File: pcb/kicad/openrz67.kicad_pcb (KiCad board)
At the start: 2 copper layers, 48 x 22 mm, 59 parts, among them U1 ESP32-C3FH4, U3 LGS5500EP, U4 S4B-XH-A(LF)(SN), U5 TLP172AM, U6 TLP172AM, X1 40MHz, X2 32.768kHz

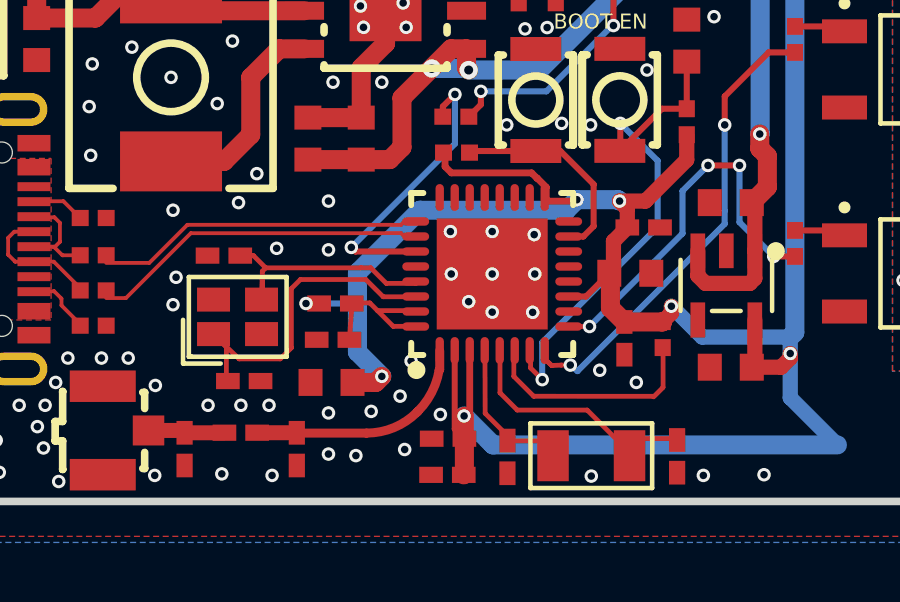
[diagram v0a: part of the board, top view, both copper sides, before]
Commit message: PCB rev 2: apply pre-fab review fixes
Blockers from the 2026-09-07 review:
- R11 100k -> 10k. It sets the LGS5500 charge current; 100k meant 1 A into
  the 250 mAh cell (rev 1 shipped like that). 10k = 400 mA per datasheet.
- Three resistor lines had 19-40 pieces in JLCPCB stock: 10k group ->
  C25744 (Basic), R12 1k -> C21190 (Basic), R18 3k -> C2909355. Library
  symbols renamed to the new MPNs, 100k symbol dropped, board fields synced.
- The VCC via feeding L2 pad 1 had its hole 0.083 mm inside the pad copper;
  moved 0.55 mm below the pad with a short F.Cu stub.

Should-fixes:
- openrz67.kicad_dru: two scoped rules instead of one unscoped one, so the
  pours stay 0.25 mm off the USB1 peg holes (rev-1 geometry) while USB1's
  own pads keep 0.17 mm.
- regen.sh: gerbers and drill use the aux origin like the CPL, so the drill
  files diff directly against the rev-1 archive; CPL rotations 0-359;
  BOM written with JLCPCB's column names and no library prefix.
- S1_DRV via nudged 0.15 mm off U1 pad 9; VDDA added to the 3v net class.

DRC 0 errors / 9 known warnings, ERC 0/0, parity clean. Every non-via
drill hole matches the rev-1 archive.
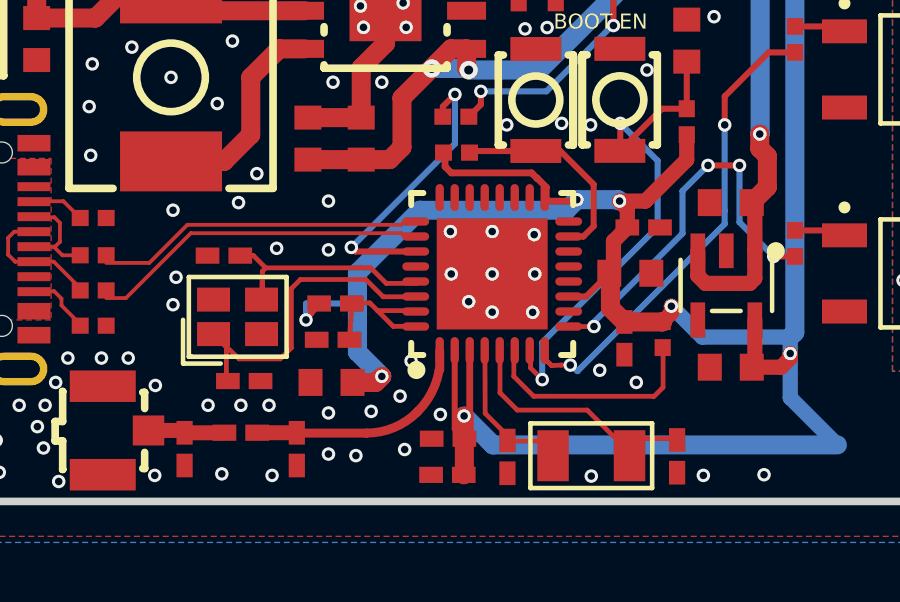
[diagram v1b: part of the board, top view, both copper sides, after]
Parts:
- R11: value 100kΩ -> 10kΩ
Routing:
- net VCC: track 93.4 -> 94.7 mm
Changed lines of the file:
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@@
 			)
 		)
-		(property "Datasheet" "https://atta.szlcsc.com/upload/public/pdf/source/20170925/C131467_1506321478108990263.pdf"
+		(property "Datasheet" "https://www.lcsc.com/product-detail/C25744.html"
 			(at 0 0 270)
 			(layer "F.Fab")
@@
 			)
 		)
-		(property "Manufacturer" "YAGEO(国巨)"
+		(property "Manufacturer" "UNI-ROYAL(厚声)"
 			(at 0 0 0)
 			(layer "F.Fab")
@@
 			)
 		)
-		(property "Manufacturer Part" "RC0402FR-0710KL"
+		(property "Manufacturer Part" "0402WGF1002TCE"
 			(at 0 0 0)
 			(layer "F.Fab")
@@
 			)
 		)
-		(property "Supplier Part" "C60490"
+		(property "Supplier Part" "C25744"
 			(at 0 0 0)
 			(layer "F.Fab")
@@
 			)
 		)
-		(property "LCSC Part Name" "厚膜电阻 10kΩ ±1% 62.5mW"
+		(property "LCSC Part Name" "10kΩ ±1% 62.5mW 厚膜电阻"
 			(at 0 0 0)
 			(layer "F.Fab")
@@
 			)
 		)
-		(property "Datasheet" "https://atta.szlcsc.com/upload/public/pdf/source/20170925/C131467_1506321478108990263.pdf"
+		(property "Datasheet" "https://www.lcsc.com/product-detail/C25744.html"
 			(at 0 0 90)
 			(layer "F.Fab")
@@
 			)
 		)
-		(property "Manufacturer" "YAGEO(国巨)"
+		(property "Manufacturer" "UNI-ROYAL(厚声)"
 			(at 0 0 0)
 			(layer "F.Fab")
@@
 			)
 		)
-		(property "Manufacturer Part" "RC0402FR-0710KL"
+		(property "Manufacturer Part" "0402WGF1002TCE"
 			(at 0 0 0)
 			(layer "F.Fab")
@@
 			)
 		)
-		(property "Supplier Part" "C60490"
+		(property "Supplier Part" "C25744"
 			(at 0 0 0)
 			(layer "F.Fab")
@@
 			)
 		)
-		(property "LCSC Part Name" "厚膜电阻 10kΩ ±1% 62.5mW"
+		(property "LCSC Part Name" "10kΩ ±1% 62.5mW 厚膜电阻"
 			(at 0 0 0)
 			(layer "F.Fab")
@@
 			)
 		)
-		(property "Datasheet" "https://atta.szlcsc.com/upload/public/pdf/source/20170925/C131467_1506321478108990263.pdf"
+		(property "Datasheet" "https://www.lcsc.com/product-detail/C25744.html"
 			(at 0 0 90)
 			(layer "F.Fab")
@@
 			)
 		)
-		(property "Manufacturer" "YAGEO(国巨)"
+		(property "Manufacturer" "UNI-ROYAL(厚声)"
 			(at 0 0 0)
 			(layer "F.Fab")
@@
 			)
 		)
-		(property "Manufacturer Part" "RC0402FR-0710KL"
+		(property "Manufacturer Part" "0402WGF1002TCE"
 			(at 0 0 0)
 			(layer "F.Fab")
@@
 			)
 		)
-		(property "Supplier Part" "C60490"
+		(property "Supplier Part" "C25744"
 			(at 0 0 0)
 			(layer "F.Fab")
@@
 			)
 		)
-		(property "LCSC Part Name" "厚膜电阻 10kΩ ±1% 62.5mW"
+		(property "LCSC Part Name" "10kΩ ±1% 62.5mW 厚膜电阻"
 			(at 0 0 0)
 			(layer "F.Fab")
@@
 			)
 		)
-		(property "Datasheet" "https://atta.szlcsc.com/upload/public/pdf/source/20170925/C131467_1506321478108990263.pdf"
+		(property "Datasheet" "https://www.lcsc.com/product-detail/C25744.html"
 			(at 0 0 0)
 			(layer "F.Fab")
@@
 			)
 		)
-		(property "Manufacturer" "YAGEO(国巨)"
+		(property "Manufacturer" "UNI-ROYAL(厚声)"
 			(at 0 0 0)
 			(layer "F.Fab")
@@
 			)
 		)
-		(property "Manufacturer Part" "RC0402FR-0710KL"
+		(property "Manufacturer Part" "0402WGF1002TCE"
 			(at 0 0 0)
 			(layer "F.Fab")
@@
 			)
 		)
-		(property "Supplier Part" "C60490"
+		(property "Supplier Part" "C25744"
 			(at 0 0 0)
 			(layer "F.Fab")
@@
 			)
 		)
-		(property "LCSC Part Name" "厚膜电阻 10kΩ ±1% 62.5mW"
+		(property "LCSC Part Name" "10kΩ ±1% 62.5mW 厚膜电阻"
 			(at 0 0 0)
 			(layer "F.Fab")
@@
 			)
 		)
-		(property "Datasheet" "https://atta.szlcsc.com/upload/public/pdf/source/20170925/C131467_1506321478108990263.pdf"
+		(property "Datasheet" "https://www.lcsc.com/product-detail/C25744.html"
 			(at 0 0 270)
 			(layer "F.Fab")
@@
 			)
 		)
-		(property "Manufacturer" "YAGEO(国巨)"
+		(property "Manufacturer" "UNI-ROYAL(厚声)"
 			(at 0 0 0)
 			(layer "F.Fab")
@@
 			)
 		)
-		(property "Manufacturer Part" "RC0402FR-0710KL"
+		(property "Manufacturer Part" "0402WGF1002TCE"
 			(at 0 0 0)
 			(layer "F.Fab")
@@
 			)
 		)
-		(property "Supplier Part" "C60490"
+		(property "Supplier Part" "C25744"
 			(at 0 0 0)
 			(layer "F.Fab")
@@
 			)
 		)
-		(property "LCSC Part Name" "厚膜电阻 10kΩ ±1% 62.5mW"
+		(property "LCSC Part Name" "10kΩ ±1% 62.5mW 厚膜电阻"
 			(at 0 0 0)
 			(layer "F.Fab")
@@
 			)
 		)
-		(property "Datasheet" "https://atta.szlcsc.com/upload/public/pdf/source/20170925/C131467_1506321478108990263.pdf"
+		(property "Datasheet" "https://www.lcsc.com/product-detail/C25744.html"
 			(at 0 0 180)
 			(layer "F.Fab")
@@
 			)
 		)
-		(property "Manufacturer" "YAGEO(国巨)"
+		(property "Manufacturer" "UNI-ROYAL(厚声)"
 			(at 0 0 0)
 			(layer "F.Fab")
@@
 			)
 		)
-		(property "Manufacturer Part" "RC0402FR-0710KL"
+		(property "Manufacturer Part" "0402WGF1002TCE"
 			(at 0 0 0)
 			(layer "F.Fab")
@@
 			)
 		)
-		(property "Supplier Part" "C60490"
+		(property "Supplier Part" "C25744"
 			(at 0 0 0)
 			(layer "F.Fab")
@@
 			)
 		)
-		(property "LCSC Part Name" "厚膜电阻 10kΩ ±1% 62.5mW"
+		(property "LCSC Part Name" "10kΩ ±1% 62.5mW 厚膜电阻"
 			(at 0 0 0)
 			(layer "F.Fab")
@@
 			)
 		)
-		(property "Datasheet" "https://atta.szlcsc.com/upload/public/pdf/source/20170925/C131467_1506321478108990263.pdf"
+		(property "Datasheet" "https://www.lcsc.com/product-detail/C25744.html"
 			(at 0 0 0)
 			(layer "F.Fab")
@@
 			)
 		)
-		(property "Manufacturer" "YAGEO(国巨)"
+		(property "Manufacturer" "UNI-ROYAL(厚声)"
 			(at 0 0 0)
 			(layer "F.Fab")
@@
 			)
 		)
-		(property "Manufacturer Part" "RC0402FR-0710KL"
+		(property "Manufacturer Part" "0402WGF1002TCE"
 			(at 0 0 0)
 			(layer "F.Fab")
@@
 			)
 		)
-		(property "Supplier Part" "C60490"
+		(property "Supplier Part" "C25744"
 			(at 0 0 0)
 			(layer "F.Fab")
@@
 			)
 		)
-		(property "LCSC Part Name" "厚膜电阻 10kΩ ±1% 62.5mW"
+		(property "LCSC Part Name" "10kΩ ±1% 62.5mW 厚膜电阻"
 			(at 0 0 0)
 			(layer "F.Fab")
@@
 			)
 		)
-		(property "Datasheet" "https://atta.szlcsc.com/upload/public/pdf/source/20200306/C422600_1E6D84923E4A46A82E41ADD87F860B5C.pdf"
+		(property "Datasheet" "https://www.lcsc.com/product-detail/C2909355.html"
 			(at 0 0 90)
 			(layer "F.Fab")
@@
 			)
 		)
-		(property "Description" "Type:Thick Film Resistors Resistance:3kΩ Tolerance:±1% Tolerance:±1% Power(Watts): Overload Voltage (Max): Temperature Coefficient:±100ppm/℃ Temperature Coefficient:±100ppm/℃ Operating Temperature Range:-55℃~+155℃ Operating Temperature Range:-55℃~+155℃"
+		(property "Description" ""
 			(at 0 0 90)
 			(layer "F.Fab")
@@
 			)
 		)
-		(property "Manufacturer" "UNI-ROYAL(厚声)"
+		(property "Manufacturer" "FOJAN"
 			(at 0 0 0)
 			(layer "F.Fab")
@@
 			)
 		)
-		(property "Manufacturer Part" "0402WGF3001TCE"
+		(property "Manufacturer Part" "FRC0402F3001TS"
 			(at 0 0 0)
 			(layer "F.Fab")
@@
 			)
 		)
-		(property "Supplier Part" "C25784"
+		(property "Supplier Part" "C2909355"
 			(at 0 0 0)
 			(layer "F.Fab")
@@
 			)
 		)
-		(property "Datasheet" "https://item.szlcsc.com/datasheet/0603WAJ0102T5E/26328.html"
+		(property "Datasheet" "https://www.lcsc.com/product-detail/C21190.html"
 			(at 0 0 270)
 			(layer "F.Fab")
@@
 			)
 		)
-		(property "Manufacturer Part" "0603WAJ0102T5E"
+		(property "Manufacturer Part" "0603WAF1001T5E"
 			(at 0 0 0)
 			(layer "F.Fab")
@@
 			)
 		)
-		(property "Supplier Part" "C25585"
+		(property "Supplier Part" "C21190"
 			(at 0 0 0)
 			(layer "F.Fab")
@@
 			)
 		)
-		(property "LCSC Part Name" "1kΩ ±5% 100mW 厚膜电阻"
+		(property "LCSC Part Name" "1kΩ ±1% 100mW 厚膜电阻"
 			(at 0 0 0)
 			(layer "F.Fab")
@@
 			)
 		)
-		(property "Value" "100kΩ"
+		(property "Value" "10kΩ"
 			(at 0 0 270)
 			(layer "F.Fab")
@@
 			)
 		)
-		(property "Datasheet" "https://item.szlcsc.com/datasheet/0402WGF1003TCE/26484.html"
+		(property "Datasheet" "https://www.lcsc.com/product-detail/C25744.html"
 			(at 0 0 270)
 			(layer "F.Fab")
@@
 			)
 		)
-		(property "Manufacturer Part" "0402WGF1003TCE"
+		(property "Manufacturer Part" "0402WGF1002TCE"
 			(at 0 0 0)
 			(layer "F.Fab")
@@
 			)
 		)
-		(property "Supplier Part" "C25741"
+		(property "Supplier Part" "C25744"
 			(at 0 0 0)
 			(layer "F.Fab")
@@
 			)
 		)
-		(property "LCSC Part Name" "100kΩ ±1% 62.5mW 厚膜电阻"
+		(property "LCSC Part Name" "10kΩ ±1% 62.5mW 厚膜电阻"
 			(at 0 0 0)
 			(layer "F.Fab")
@@
 	)
 	(segment
+		(start 135.05 105.95)
+		(end 135.487 105.4025)
+		(width 0.2)
+		(layer "F.Cu")
+		(net "VCC")
+	)
+	(segment
 		(start 144.2275 93.6535)
 		(end 144.2825 93.7085)
@@
 	)
 	(via
-		(at 135.05 105.4025)
+		(at 135.05 105.95)
 		(size 0.45)
 		(drill 0.25)
@@
 	)
 	(segment
+		(start 135.05 105.95)
+		(end 135.05 105.4025)
+		(width 0.2)
+		(layer "B.Cu")
+		(net "VCC")
+	)
+	(segment
 		(start 144.079 101.942)
 		(end 145.4545 101.942)
@@
 	(segment
 		(start 143.807 106.1695)
-		(end 144.5 106.1695)
+		(end 144.65 106.1695)
 		(width 0.16)
 		(layer "F.Cu")
@@
 	)
 	(via
-		(at 144.5 106.1695)
+		(at 144.65 106.1695)
 		(size 0.45)
 		(drill 0.25)
@@
 		(net "S1_DRV")
 	)
+	(segment
+		(start 144.65 106.1695)
+		(end 144.5 106.1695)
+		(width 0.203)
+		(layer "B.Cu")
+		(net "S1_DRV")
+	)

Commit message: PCB: unpopulated 1x4 GPIO header J1 along the bottom edge
3V3, GND, GPIO21 (U0TXD, doubles as UART TX for logging) and GPIO6 on
2.54 mm through-hole pads at x = 34.4-42.0, y = 20.3 mm, below the AGND
island so camera isolation is untouched. J1 is DNP in the schematic and on
the board, so --exclude-dnp keeps it out of the BOM and CPL; the pads are
just copper and holes on the bare PCB.

Only one right-column ESP32-C3 pin fits through the gap between the VCC,
CHIP_EN and S2_DRV tracks, the same limit the 2026-09-03 header attempt
hit; GPIO6 took it, GPIO21 escapes from the left column. Two GND stitching
vias under the pads were removed and one added at (32.8, 17.6) to reconnect
the F.Cu strip the tracks cut off. GPIO6's B.Cu detour leaves a ~57 mm2
via-stitched ground island east of U1; the flood under U1 is intact.

Footprint copied from KiCad's Connector_PinHeader_2.54mm library (3D model
reference dropped); Conn_01x04 symbol added to the project library.
DRC 0 errors / 9 known warnings, ERC 0/0, parity clean.
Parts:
- added J1: GPIO header, openrz67:PinHeader_1x04_P2.54mm_Vertical, F.Cu at (154.4, 110.3)
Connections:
- U1 pad 12: unconnected-(U1-MTCK-Pad12) -> GPIO6
- U1 pad 28: unconnected-(U1-U0TXD-Pad28) -> GPIO21
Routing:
- net GPIO6: track 0.00 -> 31.5 mm, vias 0 -> 2
- net GPIO21: track 0.00 -> 26.8 mm, vias 0 -> 4
- net VCC: track 94.7 -> 96.3 mm
- net GND: vias 108 -> 107

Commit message: PCB: silkscreen labels for J1, header moved 0.3 mm toward the edge
3V3 GND TX IO6 in two staggered rows above the pads (1.0 mm text), kept
below the U4 housing so they stay readable with the connector fitted. The
footprint's own silk outline is removed (board and library) to make room;
the square pad already marks pin 1. Pads now at y = 20.6 mm, 0.55 mm copper
to edge, and a third GND stitching via that fell within hole-to-hole
distance of pad 2 is gone. Tracks re-routed to the new pad positions.
DRC 0 errors / 9 known warnings, ERC 0/0, parity clean.
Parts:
- moved J1 0.30 mm to (154.4, 110.6)
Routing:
- net GND: vias 107 -> 106
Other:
- board text added: "3V3"
- board text added: "IO6"
- board text added: "TX"

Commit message: PCB rev 2: BQ25185 charger + TPS63031 buck-boost replace LGS5500 + LDO
The cell is rated for 120 mA charge current; the LGS5500's lowest setting is
400 mA and rev 1 shipped at 1 A. U3 is now a BQ25185DLHR (linear charger with
power path): R11 2.7 k on ISET -> 111 mA nominal, R13 18 k on ILIM/VSET -> 500 mA
input limit / 4.20 V / 3.0 V precharge, R16 NTC on TS/MR, STAT2 drives D3 (lit
while charging). SYS feeds S3 and then U2, a TPS63031DSKR fixed 3.3 V buck-boost
that replaces the ME6211 LDO (L3 2.2 uH reused, C23/C24 10 uF, C25 100 nF VINA).
LDO1, R12, R14, R17 and the +5V nets are gone. Cross-checked against the TI
datasheets; the LCSC footprints were compared with TI's land patterns.

R21/R22 220 -> 150 ohm: PhotoMOS LED current 8.2 mA worst case instead of
5.6 mA, which sat on the 5 mA minimum the 2 ohm on-resistance is specified at.

Layout cleanup after the swap: stray LCSC fields off the silkscreen, L3 net
labels matched to the routed board, U3 STAT1 pad net, L3 moved 0.25 mm off
U2's pads, GND stub to U2 pad 9, new footprints synced to the library, zones
refilled with the DRU rules. DRC 0 errors / 14 known warnings, ERC 0 errors.

CPL: ROT_FIX in regen.sh adds +90 deg for the QFN-32 (U1) and the TLP172AM
SO-4 (U5/U6), whose JLCPCB library orientation is 90 deg off the KiCad footprint
per their order preview. The rev-1 order had the same U1 offset and JLCPCB
corrected it against the silkscreen; sending the corrected angle leaves them
nothing to fix. Verify U1/U5/U6 in the preview and the DFM analysis.
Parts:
- removed LDO1: ME6211C33M5G-N, openrz67:SOT-23-5_L3.0-W1.7-P0.95-LS2.8-BL
- removed R12: 1kΩ, openrz67:R0603
- removed R14, R17: 10kΩ, openrz67:R0402
- added U2: TPS63031DSKR, openrz67:VSON-10_L2.5-W2.5-P0.50-EP1.2x2.0, F.Cu at (135.4, 98.4)
- C25: value 1uF -> 100nF; footprint openrz67:C0603 -> openrz67:C0402
- R11: value 10kΩ -> 2.7kΩ
- R13: value 10kΩ -> 18kΩ
- R21, R22: value 220Ω -> 150Ω
- U3: value LGS5500EP -> BQ25185DLHR; footprint openrz67:ESOP-8_L4.9-W3.9-P1.27-LS6.0-TL-EP3.3 -> openrz67:WSON-10_L2.2-W2.0-P0.40-EP0.9x1.5
- moved C25 11.4 mm to (138.0, 99.8), turned to 180 degrees
- moved C22 6.05 mm to (131.8, 91.5)
- moved C24 4.17 mm to (139.3, 96.5)
- moved D3 2.97 mm to (140.5, 94.0), turned to 90 degrees
- moved R18 2.55 mm to (142.0, 92.8)
- moved C23 2.04 mm to (136.5, 101.4), turned to 0 degrees
- moved R11 1.61 mm to (134.2, 91.0), turned to 180 degrees
- moved U3 1.49 mm to (137.0, 93.7)
- moved R16 1.12 mm to (138.7, 91.0)
- moved R13 0.66 mm to (136.2, 91.0), turned to 180 degrees
- moved L3 0.25 mm to (130.3, 97.9)
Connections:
- net Net-(D3-A) renamed LED_A
- C22 pad 2: BAT+ -> VSYS
- C23 pad 2: +5V -> SW_SYS
- C24 pad 2: +5V -> VCC
- C25 pad 2: +5V_VIN -> SW_SYS
- D3 pad 1: GND -> STAT2
- L3 pad 1: BAT+ -> SW2
- L3 pad 2: Net-(U3-LX) -> SW1
- R11 pad 1: GND -> ISET
- R11 pad 2: Net-(U3-ISET) -> GND
- R13 pad 1: VBUS -> ILIM_VSET
- R13 pad 2: Net-(U3-NTC) -> GND
- R16 pad 1: Net-(U3-NTC) -> TS_MR
- R18 pad 1: Net-(U3-VSET_(LED)) -> VSYS
- S3 pad 1: +5V -> VSYS
- S3 pad 2: +5V_VIN -> SW_SYS
- U3 pad 1: Net-(U3-ISET) -> VSYS
- U3 pad 2: VBUS -> BAT+
- U3 pad 3: BAT+ -> STAT2
- U3 pad 4: Net-(U3-LX) -> GND
- U3 pad 5: +5V -> GND
- U3 pad 6: unconnected-(U3-NC-Pad6) -> TS_MR
- U3 pad 7: Net-(U3-VSET_(LED)) -> ILIM_VSET
- U3 pad 8: Net-(U3-NTC) -> ISET
- U3 pad 9: GND -> unconnected-(U3-STAT1-Pad9)
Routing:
- net SW_SYS: track 0.00 -> 29.1 mm, vias 0 -> 2
- net VSYS: track 0.00 -> 23.2 mm, vias 0 -> 4
- net VCC: track 96.4 -> 116.6 mm, vias 8 -> 9
- net +5V: track 19.7 -> 0.00 mm, vias 2 -> 0
- net +5V_VIN: track 16.2 -> 0.00 mm, vias 2 -> 0
- net Net-(U3-LX): track 7.12 -> 0.00 mm
- net Net-(U3-NTC): track 6.36 -> 0.00 mm
- net GND: track 6.31 -> 1.40 mm, vias 106 -> 74
- net SW2: track 0.00 -> 4.82 mm
- net STAT2: track 0.00 -> 4.62 mm
- net SW1: track 0.00 -> 4.50 mm
- net ISET: track 0.00 -> 4.02 mm
- net VBUS: track 33.9 -> 30.0 mm, vias 0 -> 2
- net Net-(U3-VSET_(LED)): track 3.50 -> 0.00 mm
- net Net-(U3-ISET): track 2.54 -> 0.00 mm
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
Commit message: PCB: R20 1 kOhm, J1 excluded from BOM/CPL by attribute, 3D model fixes, MPN
- R20 10k -> 1k (C11702): the blue status LED was practically invisible.
- J1: in_bom no on the symbol, exclude_from_bom/exclude_from_pos_files on the
  footprint, so the exclusion no longer hinges on --exclude-dnp.
- TLP172AM MPN 'TLP172AM(TPL,E' -> 'TLP172AM(TPL,E)'.
- 3D models: the imported offsets put U4 3.45 mm off and 3.4 mm low, BAT1/S3
  0.6 mm off and 3.5 mm low, USB1 1.2 mm off and 0.9 mm low (checked against the
  pin geometry in the .wrl files). Corrected in the library and the board; the
  BQ25185 and TPS63031 got their LCSC models.
DRC 0 errors / 14 known warnings, ERC 0 errors.
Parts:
- R20: value 10kΩ -> 1kΩ
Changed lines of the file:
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@@
 		)
 		(embedded_fonts no)
+		(model "${KIPRJMOD}/openrz67.3dshapes/SON-10_L2.5-W2.5-H0.8-P0.50.wrl"
+			(offset
+				(xyz 0 0 0)
+			)
+			(scale
+				(xyz 1 1 1)
+			)
+			(rotate
+				(xyz 0 0 0)
+			)
+		)
 	)
 	(footprint "openrz67:C0402"
@@
 			)
 		)
-		(property "Value" "10kΩ"
+		(property "Value" "1kΩ"
 			(at 0 0 0)
 			(layer "F.Fab")
@@
 			)
 		)
-		(property "Manufacturer Part" "0402WGF1002TCE"
+		(property "Manufacturer Part" "0402WGF1001TCE"
 			(at 0 0 0)
 			(layer "F.Fab")
@@
 			)
 		)
-		(property "Supplier Part" "C25744"
+		(property "Supplier Part" "C11702"
 			(at 0 0 0)
 			(layer "F.Fab")
@@
 			)
 		)
-		(property "LCSC Part Name" "10kΩ ±1% 62.5mW 厚膜电阻"
+		(property "LCSC Part Name" "1kΩ ±1% 62.5mW"
 			(at 0 0 0)
 			(layer "F.Fab")
@@
 		(model "${KIPRJMOD}/openrz67.3dshapes/CONN-TH_PH2.00-LI-2P.wrl"
 			(offset
-				(xyz 0 0.6 -3.5)
+				(xyz 0 1.2 0)
 			)
 			(scale
@@
 			)
 			(rotate
-				(xyz -0 -0 -180)
+				(xyz 0 0 180)
 			)
 		)
@@
 		(model "${KIPRJMOD}/openrz67.3dshapes/CONN-TH_PH2.00-LI-2P.wrl"
 			(offset
-				(xyz 0 0.6 -3.5)
+				(xyz 0 1.2 0)
 			)
 			(scale
@@
 			)
 			(rotate
-				(xyz -0 -0 -180)
+				(xyz 0 0 180)
 			)
 		)
@@
 		(model "${KIPRJMOD}/openrz67.3dshapes/CONN-TH_S4B-XH-A-LF-SN.wrl"
 			(offset
-				(xyz 0.015 3.464 -3.4)
+				(xyz 0 6.91 0)
 			)
 			(scale
@@
 			)
 			(rotate
-				(xyz -0 -0 -180)
+				(xyz 0 0 180)
 			)
 		)
@@
 			)
 		)
-		(property "Manufacturer Part" "TLP172AM(TPL,E"
+		(property "Manufacturer Part" "TLP172AM(TPL,E)"
 			(at 0 0 180)
 			(layer "F.Fab")
@@
 			)
 		)
-		(property "LCSC Part Name" "TLP172AM(TPL,E"
+		(property "LCSC Part Name" "TLP172AM(TPL,E)"
 			(at 0 0 180)
 			(layer "F.Fab")
@@
 		(model "${KIPRJMOD}/openrz67.3dshapes/USB-C-SMD_TYPE-C-6PIN-2MD-073.wrl"
 			(offset
-				(xyz 0 -1.2 -0.9)
+				(xyz 0 0 0)
 			)
 			(scale
@@
 			)
 			(rotate
-				(xyz -0 -0 -0)
+				(xyz 0 0 0)
 			)
 		)
@@
 			)
 		)
-		(property "Manufacturer Part" "TLP172AM(TPL,E"
+		(property "Manufacturer Part" "TLP172AM(TPL,E)"
 			(at 0 0 180)
 			(layer "F.Fab")
@@
 			)
 		)
-		(property "LCSC Part Name" "TLP172AM(TPL,E"
+		(property "LCSC Part Name" "TLP172AM(TPL,E)"
 			(at 0 0 180)
 			(layer "F.Fab")
@@
 			)
 		)
-		(attr through_hole dnp)
+		(attr through_hole exclude_from_pos_files exclude_from_bom dnp)
 		(duplicate_pad_numbers_are_jumpers no)
 		(fp_rect
@@
 		)
 		(embedded_fonts no)
+		(model "${KIPRJMOD}/openrz67.3dshapes/WSON-10_L2.2-W2.0-P0.40-BL-EP_TI_DLH0010A.wrl"
+			(offset
+				(xyz 0 0 0)
+			)
+			(scale
+				(xyz 1 1 1)
+			)
+			(rotate
+				(xyz 0 0 270)
+			)
+		)
 	)
 	(footprint "openrz67:C0603"
